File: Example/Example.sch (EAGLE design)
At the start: 28 parts, among them IC2 74LS02D, IC3 74LS02D, U1 CD4017

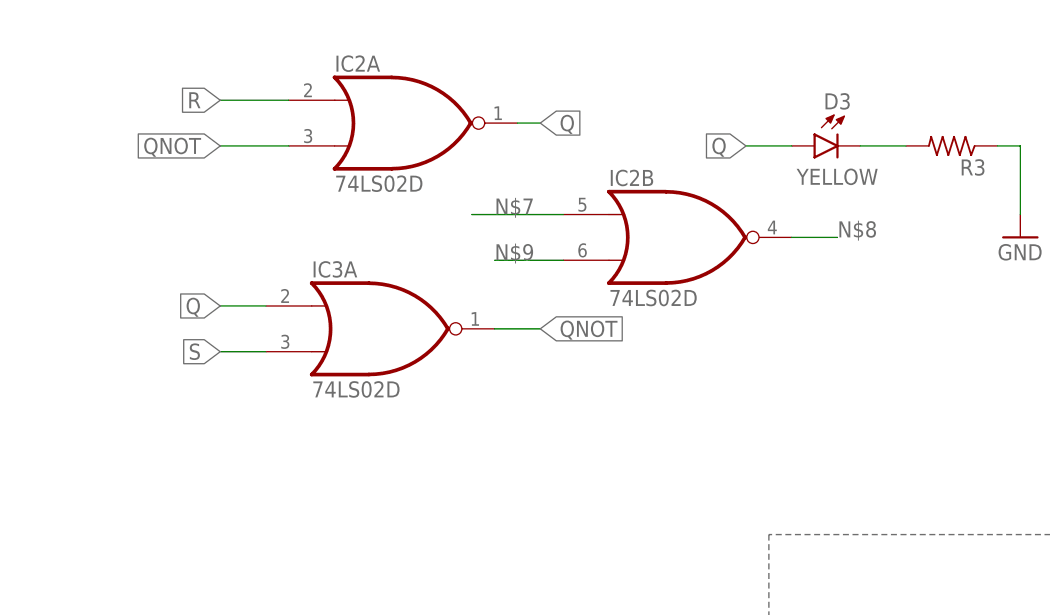
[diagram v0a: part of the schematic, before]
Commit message: Fixed multiple NOR gate issue
Removed IC3A from the schematic
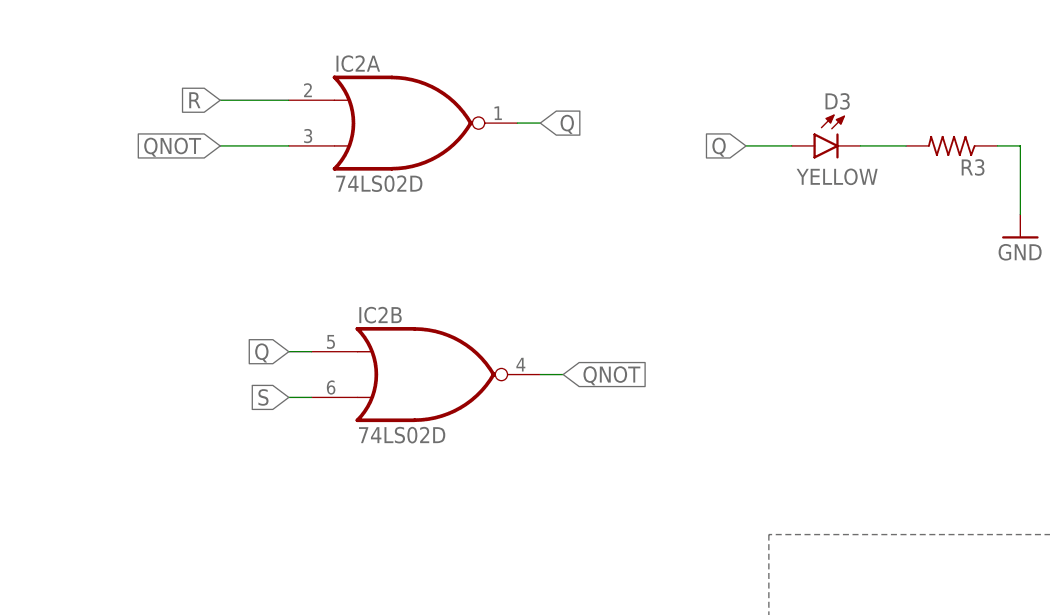
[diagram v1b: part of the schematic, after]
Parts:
- removed IC3: 74LS02D, 74xx-us:74LS02D
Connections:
- removed net N$7: IC2B.I0
- removed net N$8: IC2B.O
- removed net N$9: IC2B.I1
- net Q: now also IC2B.I0; no longer IC3A.I0
- net QNOT: now also IC2B.O; no longer IC3A.O
- net S: now also IC2B.I1; no longer IC3A.I1
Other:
- moved on the sheet: IC2B
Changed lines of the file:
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@@
 <?xml version="1.0" encoding="utf-8"?>
 <!DOCTYPE eagle SYSTEM "eagle.dtd">
-<eagle version="9.5.1">
+<eagle version="9.5.2">
 <drawing>
 <settings>
@@
 <part name="S1" library="adafruit" library_urn="urn:adsk.eagle:library:420" deviceset="40-XX" device="-ROUND" package3d_urn="urn:adsk.eagle:package:6240926/1"/>
 <part name="U$1" library="adafruit" library_urn="urn:adsk.eagle:library:420" deviceset="CR1220" device="SMT" package3d_urn="urn:adsk.eagle:package:6240665/1"/>
-<part name="IC3" library="74xx-us" library_urn="urn:adsk.eagle:library:88" deviceset="74*02" device="D" package3d_urn="urn:adsk.eagle:package:2917/1" technology="LS"/>
 <part name="D2" library="RoboJackets-LEDs" deviceset="LED-SMD" device="" technology="-YELLOW" value="YELLOW"/>
 <part name="D3" library="RoboJackets-LEDs" deviceset="LED-SMD" device="" technology="-YELLOW" value="YELLOW"/>
@@
 <attribute name="VALUE" x="29.21" y="99.06" size="1.778" layer="96"/>
 </instance>
-<instance part="IC3" gate="A" x="111.76" y="78.74" smashed="yes">
-<attribute name="NAME" x="104.14" y="84.455" size="1.778" layer="95"/>
-<attribute name="VALUE" x="104.14" y="71.12" size="1.778" layer="96"/>
-</instance>
 <instance part="D2" gate="A" x="243.84" y="119.38" smashed="yes">
 <attribute name="NAME" x="243.84" y="123.444" size="1.778" layer="95" rot="MR0" align="bottom-center"/>
@@
 <attribute name="VALUE" x="17.78" y="83.82" size="1.778" layer="96"/>
 </instance>
-<instance part="IC2" gate="B" x="144.78" y="88.9" smashed="yes">
-<attribute name="NAME" x="137.16" y="94.615" size="1.778" layer="95"/>
-<attribute name="VALUE" x="137.16" y="81.28" size="1.778" layer="96"/>
+<instance part="IC2" gate="B" x="116.84" y="73.66" smashed="yes">
+<attribute name="NAME" x="109.22" y="79.375" size="1.778" layer="95"/>
+<attribute name="VALUE" x="109.22" y="66.04" size="1.778" layer="96"/>
 </instance>
 <instance part="U1" gate="G1" x="60.96" y="172.72" smashed="yes">
@@
 </segment>
 <segment>
-<pinref part="IC3" gate="A" pin="O"/>
-<wire x1="124.46" y1="78.74" x2="129.54" y2="78.74" width="0.1524" layer="91"/>
-<label x="129.54" y="78.74" size="1.778" layer="95" xref="yes"/>
+<label x="132.08" y="73.66" size="1.778" layer="95" xref="yes"/>
+<pinref part="IC2" gate="B" pin="O"/>
+<wire x1="132.08" y1="73.66" x2="129.54" y2="73.66" width="0.1524" layer="91"/>
 </segment>
 </net>
@@
 <net name="Q" class="0">
 <segment>
-<pinref part="IC3" gate="A" pin="I0"/>
-<wire x1="99.06" y1="81.28" x2="93.98" y2="81.28" width="0.1524" layer="91"/>
-<label x="93.98" y="81.28" size="1.778" layer="95" rot="R180" xref="yes"/>
+<label x="101.6" y="76.2" size="1.778" layer="95" rot="R180" xref="yes"/>
+<pinref part="IC2" gate="B" pin="I0"/>
+<wire x1="104.14" y1="76.2" x2="101.6" y2="76.2" width="0.1524" layer="91"/>
 </segment>
 <segment>
@@
 <net name="S" class="0">
 <segment>
-<pinref part="IC3" gate="A" pin="I1"/>
-<wire x1="99.06" y1="76.2" x2="93.98" y2="76.2" width="0.1524" layer="91"/>
-<label x="93.98" y="76.2" size="1.778" layer="95" rot="R180" xref="yes"/>
+<label x="101.6" y="71.12" size="1.778" layer="95" rot="R180" xref="yes"/>
+<pinref part="IC2" gate="B" pin="I1"/>
+<wire x1="104.14" y1="71.12" x2="101.6" y2="71.12" width="0.1524" layer="91"/>
 </segment>
 <segment>
@@
 </segment>
 </net>
-<net name="N$7" class="0">
-<segment>
-<pinref part="IC2" gate="B" pin="I0"/>
-<wire x1="132.08" y1="91.44" x2="121.92" y2="91.44" width="0.1524" layer="91"/>
-<label x="124.46" y="91.44" size="1.778" layer="95"/>
-</segment>
-</net>
-<net name="N$8" class="0">
-<segment>
-<pinref part="IC2" gate="B" pin="O"/>
-<wire x1="157.48" y1="88.9" x2="162.56" y2="88.9" width="0.1524" layer="91"/>
-<label x="162.56" y="88.9" size="1.778" layer="95"/>
-</segment>
-</net>
-<net name="N$9" class="0">
-<segment>
-<pinref part="IC2" gate="B" pin="I1"/>
-<wire x1="132.08" y1="86.36" x2="124.46" y2="86.36" width="0.1524" layer="91"/>
-<label x="124.46" y="86.36" size="1.778" layer="95"/>
-</segment>
-</net>
